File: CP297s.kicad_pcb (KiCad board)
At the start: 2 copper layers, 155.1 x 156 mm, 124 parts, among them J1 Conn_01x05_Male, J2 Conn_01x04_Female, J3 pin header 01x15 2.54mm, J4 Conn_01x06_Female, J5 PG203J, J6 PG203J, J7 PG203J, K1 CONN_3, K2 CONN_3, K3 TK85_BUS, P2 CONN_2, P6 CONN_2, U1 Z80, U10 74LS125, U11 74LS393, U12 74LS574, U13 74LS08, U14 74LS251, U15 74HC86, U16 74LS245, U17 74LS32, U18 74HCT00, U19 74LS138, U2 62256, U20 74HC74, U21 74HC74, U22 74LS165, U23 74LS32, U24 AY-3-8910, U25 74LS08, U26 74LS138, U3 27256, U4 74HC04, U5 74HC74, U6 74LS393, U7 74LS11, U8 74LS32, U9 74LS245, X1 6.5MHz

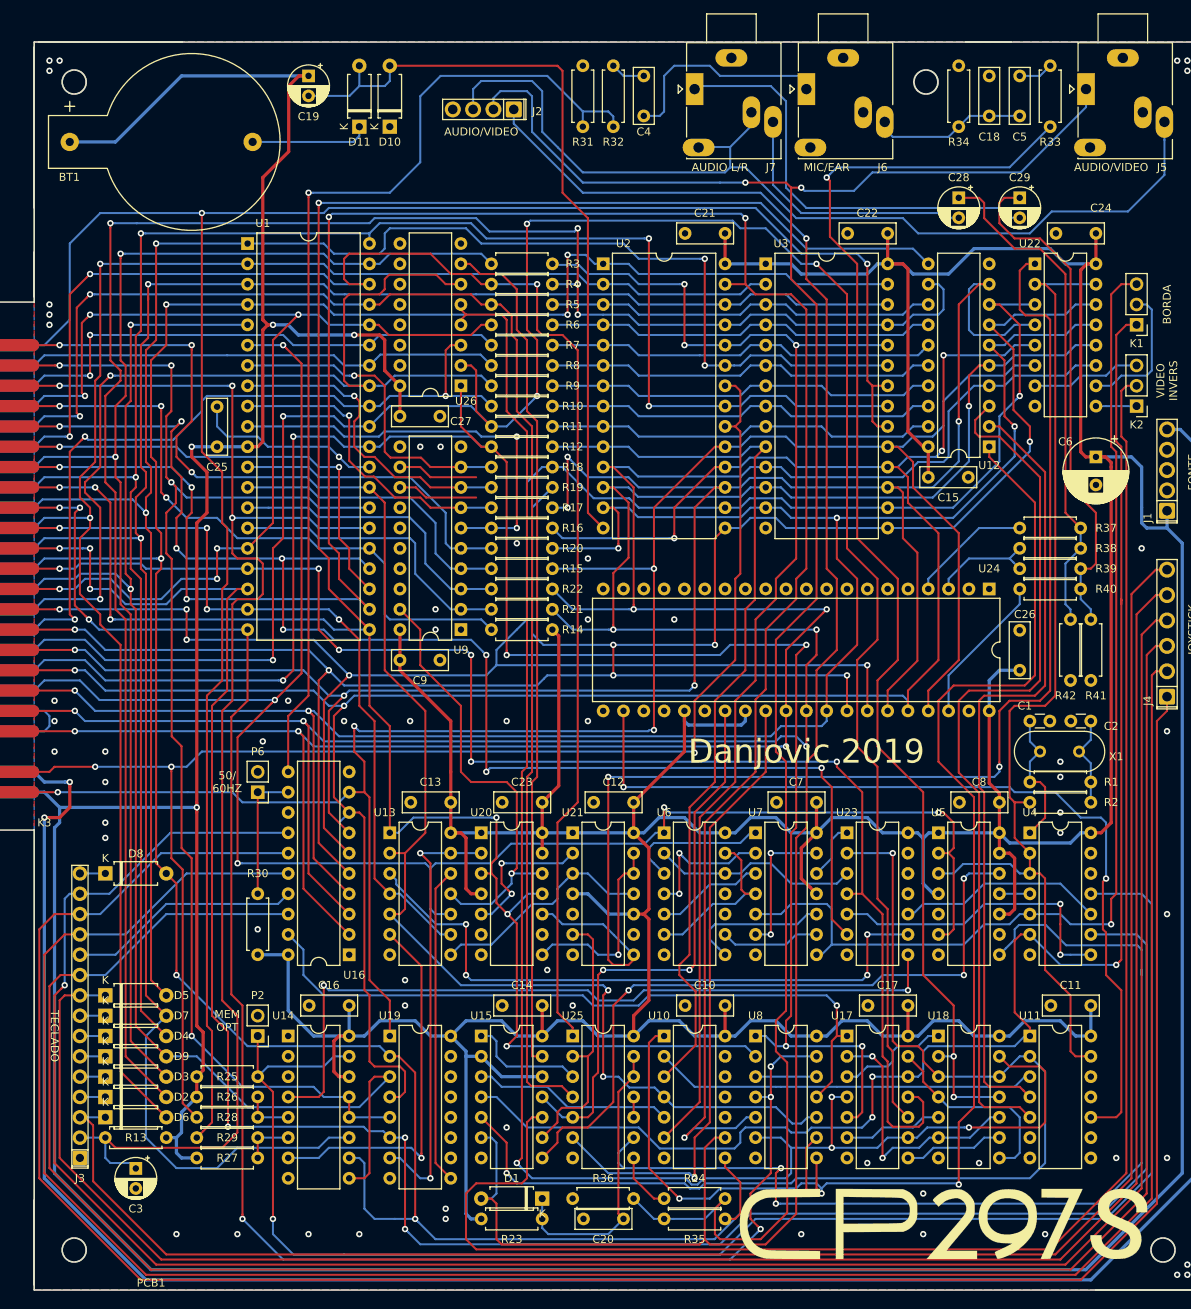
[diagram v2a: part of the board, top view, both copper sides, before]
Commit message: moved battery clip, substituted audio-mono for +5Vcc at MONITOR OUT connector
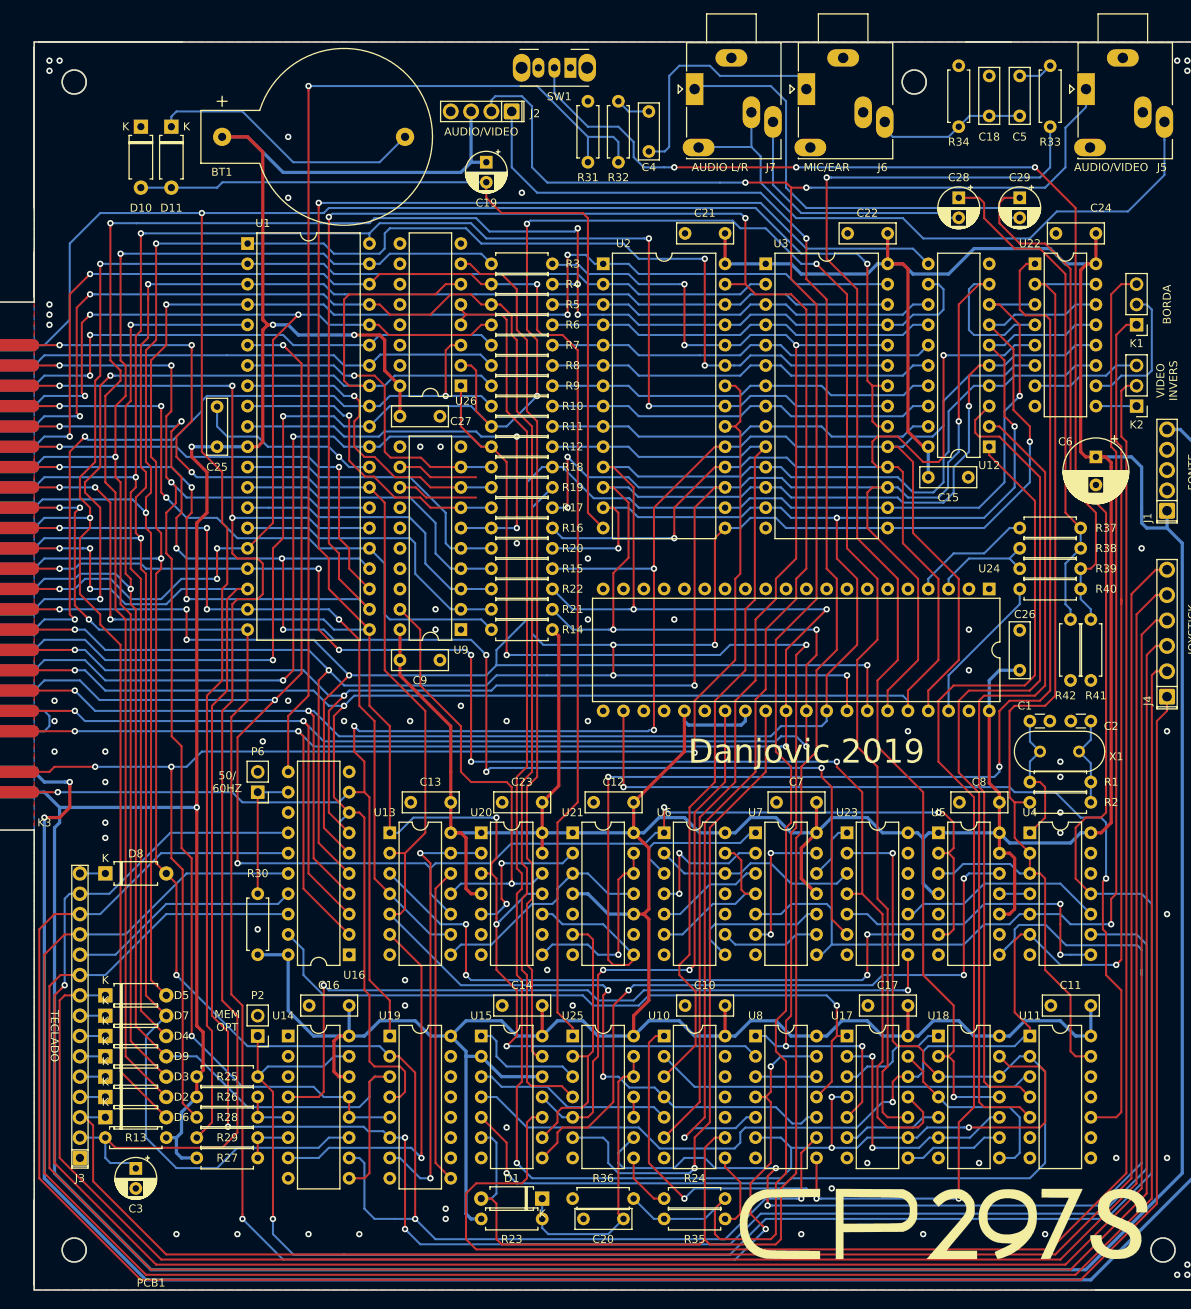
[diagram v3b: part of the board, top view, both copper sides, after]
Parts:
- removed LOGO1: LOGO, CP297s:logo
- added G***: LOGO, CP297s:logo, F.Cu at (139.1, 194.9)
- added SW1: SW_SPDT, Button_Switch_THT:SW_CuK_OS102011MA1QN1_SPDT_Angled, F.Cu at (92.4, 50.4)
- moved D10 31.1 mm to (38.7, 57.8), turned to 270 degrees
- moved C19 24.7 mm to (81.9, 62.2)
- moved D11 23.5 mm to (42.5, 57.8), turned to 270 degrees
- moved BT1 19.1 mm to (48.9, 59.1)
- moved C4 4.49 mm to (102.2, 55.9)
- moved R31 4.49 mm to (94.6, 62.2)
- moved R32 4.49 mm to (98.4, 62.2)
- moved J2 0.36 mm to (85.1, 55.9)
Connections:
- J2 pad 3: AUDIO-MONO -> +5V
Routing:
- net Net-(P2-Pad1): track 195.0 -> 361.2 mm, vias 1 -> 4
- net AUDIO-MONO: track 122.4 -> 79.2 mm
- net Net-(BT1-Pad2): track 14.8 -> 34.7 mm
- net A8: track 193.2 -> 183.2 mm
- net D6': track 287.9 -> 296.4 mm, vias 5 -> 4
- net Net-(R31-Pad1): track 127.7 -> 134.1 mm
- net /VIDEO: track 252.6 -> 258.0 mm
- net D5': track 265.1 -> 269.9 mm
- net ~CSYNC: track 241.6 -> 245.5 mm
- net /EAR: track 27.3 -> 31.1 mm
- net D0': track 269.1 -> 272.2 mm
- net ~SEROUT: track 161.8 -> 164.7 mm, vias 3 -> 2
- net D2': track 255.2 -> 257.4 mm
- net D3': track 273.5 -> 275.7 mm
- net ~: track 96.5 -> 98.7 mm
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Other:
- outline, holes or cut-outs redrawn

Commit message: updated board outline, support for external kolour
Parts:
- SW1: footprint Button_Switch_THT:SW_CuK_OS102011MA1QN1_SPDT_Angled -> CP297s:SS-12F23_SPDT_Angled
- moved C19 31.8 mm to (50.2, 64.1)
- moved C4 5.12 mm to (97.8, 58.4)
- moved R31 5.12 mm to (90.2, 64.8)
- moved R32 5.12 mm to (94.0, 64.8)
- moved SW1 3.81 mm to (90.4, 53.7)
- moved J2 3.17 mm to (85.1, 59.1)
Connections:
- J1 pad 5: +9V -> /+9V
- J2 pad 2: /VIDEO -> /RAW_VIDEO
- J5 pad 2: AUDIO-MONO -> /AUDIO-MONO
- R24 pad 2: Net-(R24-Pad2) -> /RAW_VIDEO
- U11 pad 13: 6.5M -> /6.5M
- U25 pad 4: A7 -> /A7
- U25 pad 8: Net-(R24-Pad2) -> /RAW_VIDEO
- U26 pad 1: A0 -> /A0
- U26 pad 2: A1 -> /A1
- U26 pad 3: A2 -> /A2
- U26 pad 5: ~IOWR -> /~IOWR
- U26 pad 6: A3 -> /A3
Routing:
- net /+9V: track 0.00 -> 306.8 mm, vias 0 -> 2
- net +9V: track 306.8 -> 0.00 mm, vias 2 -> 0
- net /RAW_VIDEO: track 0.00 -> 157.0 mm, vias 0 -> 1
- net /VIDEO: track 258.0 -> 206.4 mm, vias 2 -> 1
- net Net-(R24-Pad2): track 7.40 -> 0.00 mm
- net +5V: track 1168.9 -> 1163.3 mm
- net /EAR: track 31.1 -> 36.6 mm
- net D7': track 257.4 -> 261.2 mm
- net Net-(BT1-Pad2): track 34.7 -> 31.3 mm
- net Net-(U20-Pad8): track 24.7 -> 21.5 mm
- net ~CSYNC: track 245.5 -> 242.4 mm
- net Net-(R31-Pad1): track 134.1 -> 131.2 mm
- net Net-(U20-Pad10): track 162.7 -> 164.7 mm
- net Net-(U15-Pad11): track 71.6 -> 70.2 mm
- net Net-(R35-Pad1): track 9.94 -> 8.67 mm
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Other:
- outline, holes or cut-outs redrawn
- board text added: "MONITOR"

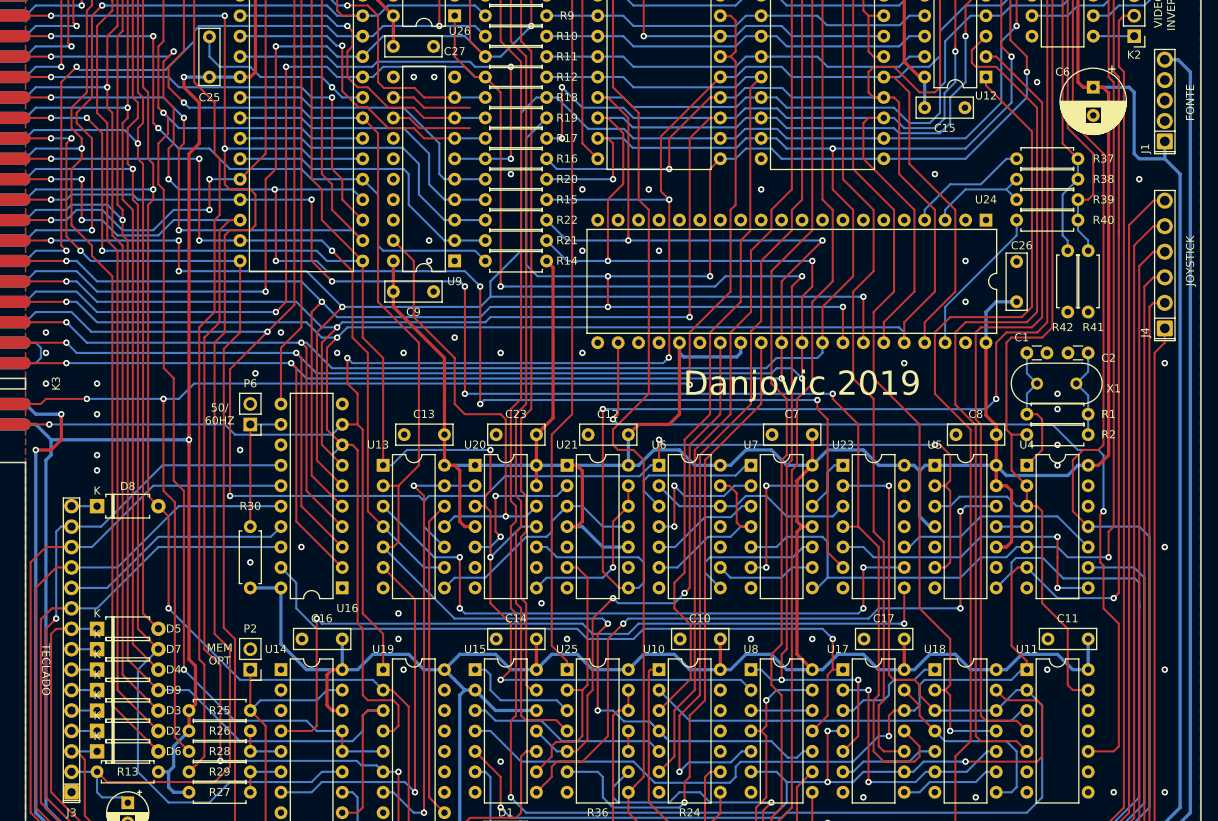
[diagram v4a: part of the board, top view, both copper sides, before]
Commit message: Added resistor network at keyboard inputs
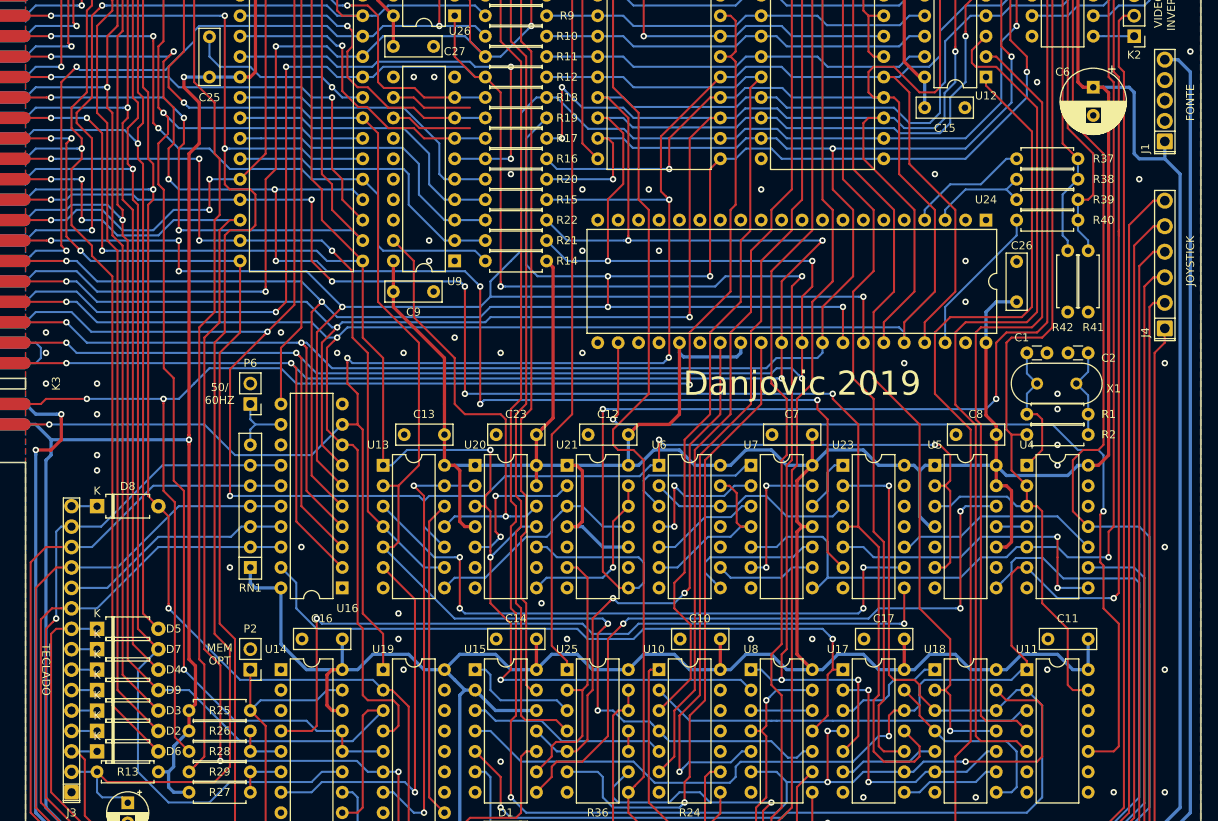
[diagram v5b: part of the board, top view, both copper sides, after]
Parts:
- removed R30: 10K, Resistor_THT:R_Axial_DIN0207_L6.3mm_D2.5mm_P7.62mm_Horizontal
- added RN1: 47k, Resistor_THT:R_Array_SIP7, F.Cu at (53.3, 158.8)
- moved P6 2.54 mm to (53.3, 138.4)
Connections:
- U15 pad 9: INVERT -> /INVERT
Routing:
- net Net-(P6-Pad1): track 16.5 -> 8.78 mm
- net +5V: track 1163.3 -> 1165.5 mm
- net D7': track 261.2 -> 263.3 mm
- net D6': track 296.4 -> 294.6 mm
- net ~RAMCS: track 180.4 -> 181.9 mm
- net A15: track 172.4 -> 171.2 mm
- net GND: vias 89 -> 88

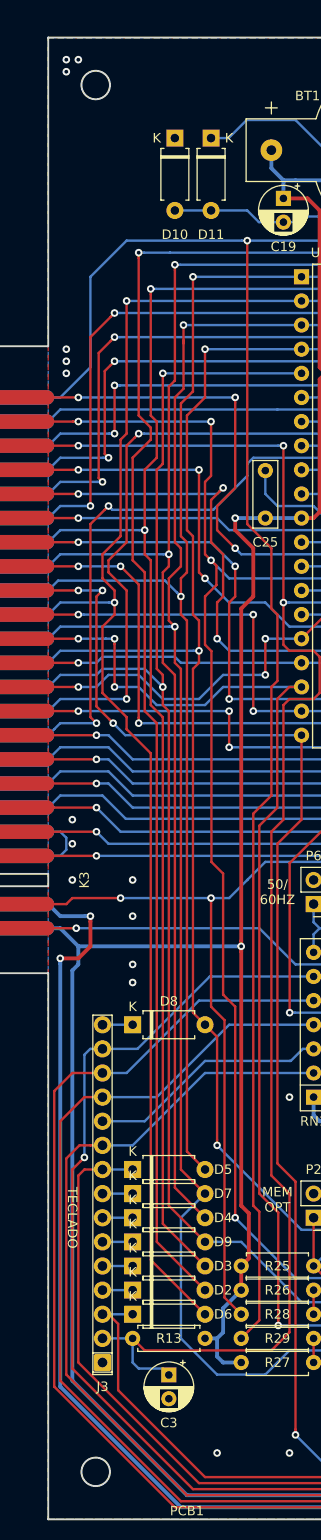
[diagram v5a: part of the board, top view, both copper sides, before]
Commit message: added revision version in top silk
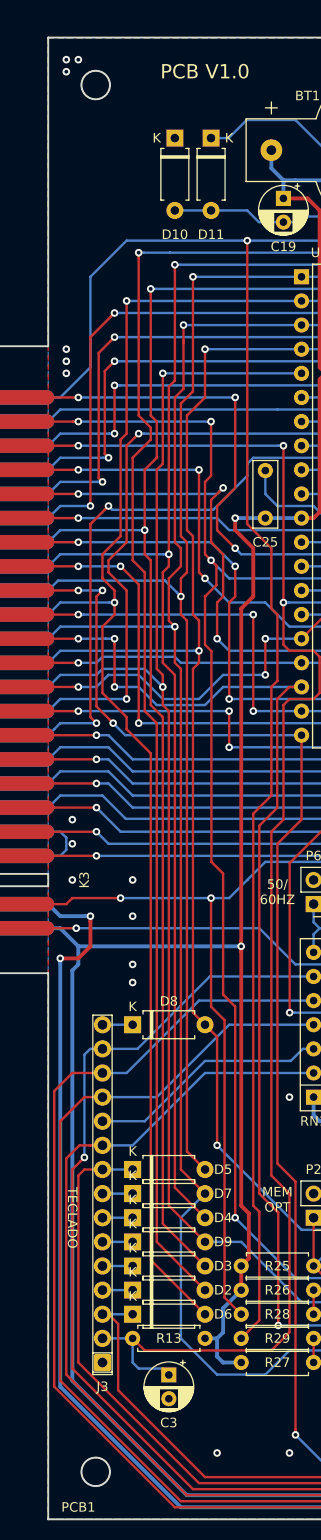
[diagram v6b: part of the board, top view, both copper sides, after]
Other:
- board text added: "PCB V1.0"
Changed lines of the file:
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@@
   (general
     (thickness 1.6)
-    (drawings 13)
+    (drawings 14)
     (tracks 3213)
     (modules 125)
@@
   (page "A4" portrait)
   (layers
-    (0 "F.Cu" signal)
-    (31 "B.Cu" signal)
+    (0 "F.Cu" signal hide)
+    (31 "B.Cu" signal hide)
     (32 "B.Adhes" user)
     (33 "F.Adhes" user)
@@
   (module "CP297s:Placa_CP200S" locked (layer "F.Cu")
     (at 25.4 203.2)
-    (fp_text reference "PCB1" (at 14.605 -0.889) (layer "F.SilkS")
+    (fp_text reference "PCB1" (at 3.175 -1.27) (layer "F.SilkS")
       (effects (font (size 1 1) (thickness 0.15)))
     )
@@
       (xy -15.4305 -3.378654)) (layer "F.SilkS") (width 0.01))
   )
+  (gr_text "PCB V1.0" (at 41.91 50.8) (layer "F.SilkS")
+    (effects (font (size 1.5 1.5) (thickness 0.25)))
+  )
   (gr_text "MEM\nOPT" (at 99.06 49.53) (layer "F.SilkS")

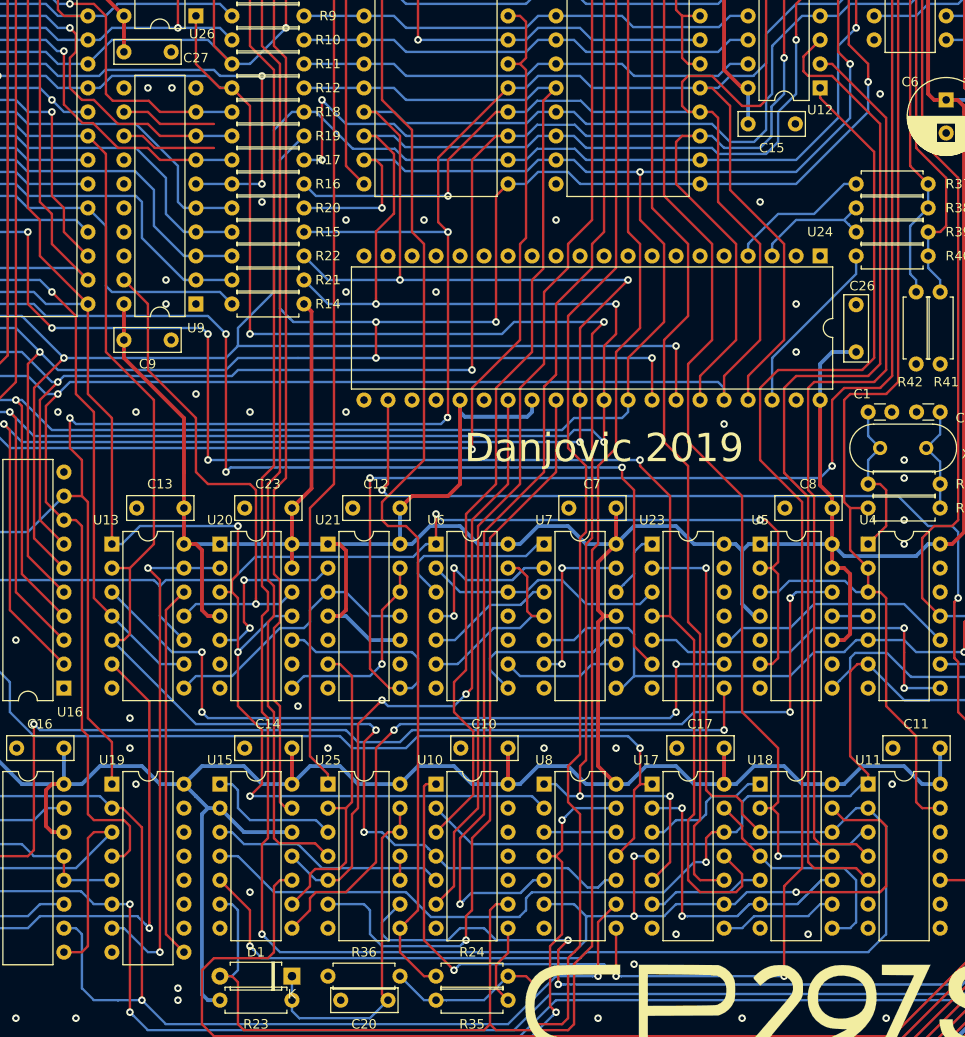
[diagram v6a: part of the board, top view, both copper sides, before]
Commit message: fixed CPU syncrhonizer (/wait logic)
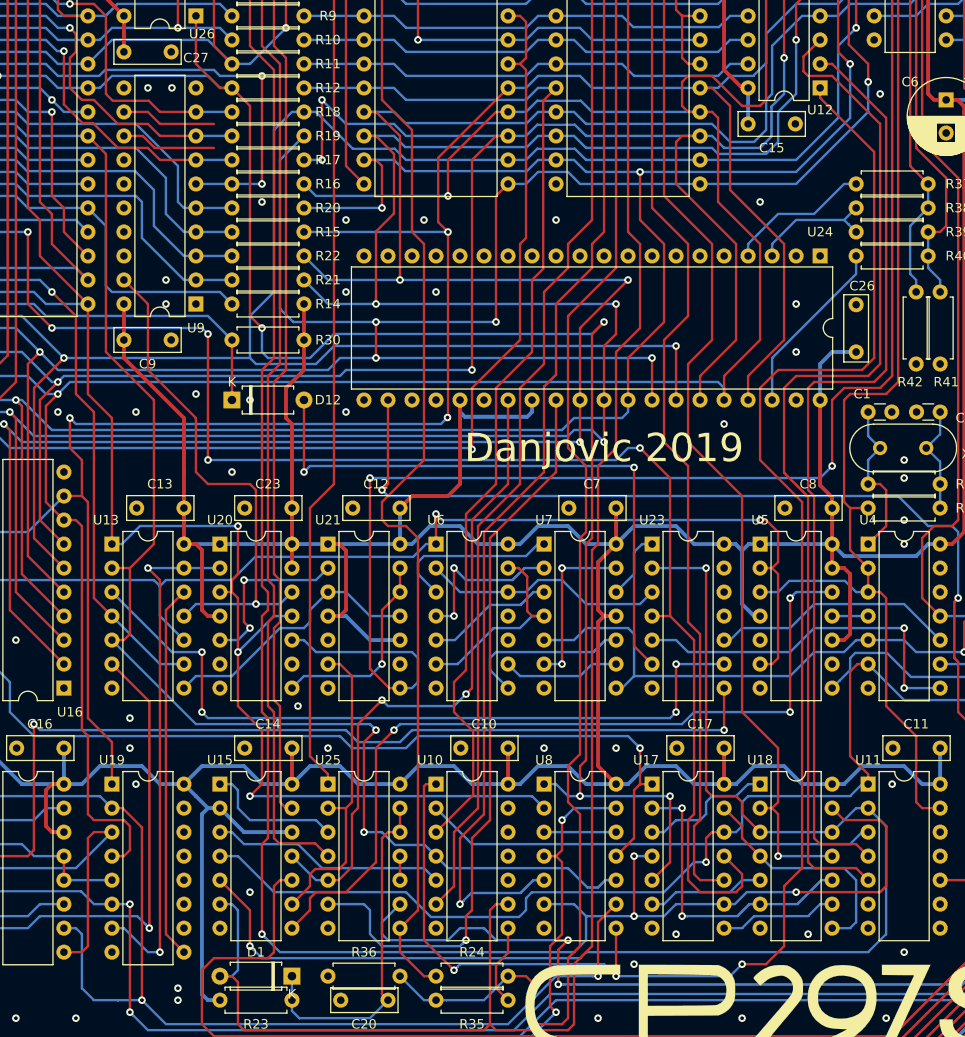
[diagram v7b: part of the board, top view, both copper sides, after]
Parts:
- added D12: 4148, Diode_THT:D_A-405_P7.62mm_Horizontal, F.Cu at (82.5, 130.8)
- added R30: 10K, Resistor_THT:R_Axial_DIN0207_L6.3mm_D2.5mm_P7.62mm_Horizontal, F.Cu at (90.2, 124.5)
- D1: value DIODE -> 4148
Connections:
- U23 pad 6: ~WAIT -> Net-(D12-Pad2)
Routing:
- net ~WAIT: track 175.6 -> 104.0 mm, vias 8 -> 5
- net Net-(D12-Pad2): track 0.00 -> 64.5 mm, vias 0 -> 2
- net A0: track 240.2 -> 242.7 mm
- net Net-(U10-Pad1): track 172.1 -> 170.3 mm
- net ~NMI: track 182.6 -> 184.4 mm
- net D4': track 259.9 -> 261.1 mm
- net GND: vias 88 -> 89
